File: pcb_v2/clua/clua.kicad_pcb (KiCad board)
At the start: 2 copper layers, 160.7 x 210 mm, 86 parts, among them J1 bus clu 1, J11 UCODE_1, J12 UCODE_2, J13 UCODE_3, J14 UCODE_4, J15 UCODE_5, J16 UCODE_6, J17 UCODE_7, J18 UCODE_INT, J2 bus clu 2, J3 bus clu 3, J4 UCODE_RESET, J7 UCODE_0, SW1 SW_DIP_x04, SW3 SW_DIP_x04, SW6 SW_DIP_x04, U1 74LS193, U10 MC14495P, U11 IR_HIGH, U12 74LS574, U13 74LS244, U15 74LS244, U16 74LS86, U17 74LS125, U18 74LS244, U19 74LS04, U2 74HC238, U20 74LS08, U24 74LS86, U25 74LS125, U26 74LS32, U27 74LS08, U28 74LS74, U29 74LS74, U30 74LS138, U31 MC14495P, U32 74HC238, U4 74LS02, U5 74LS32, U6 74LS157, U7 74LS157, U8 74LS574, U9 IR_LOW

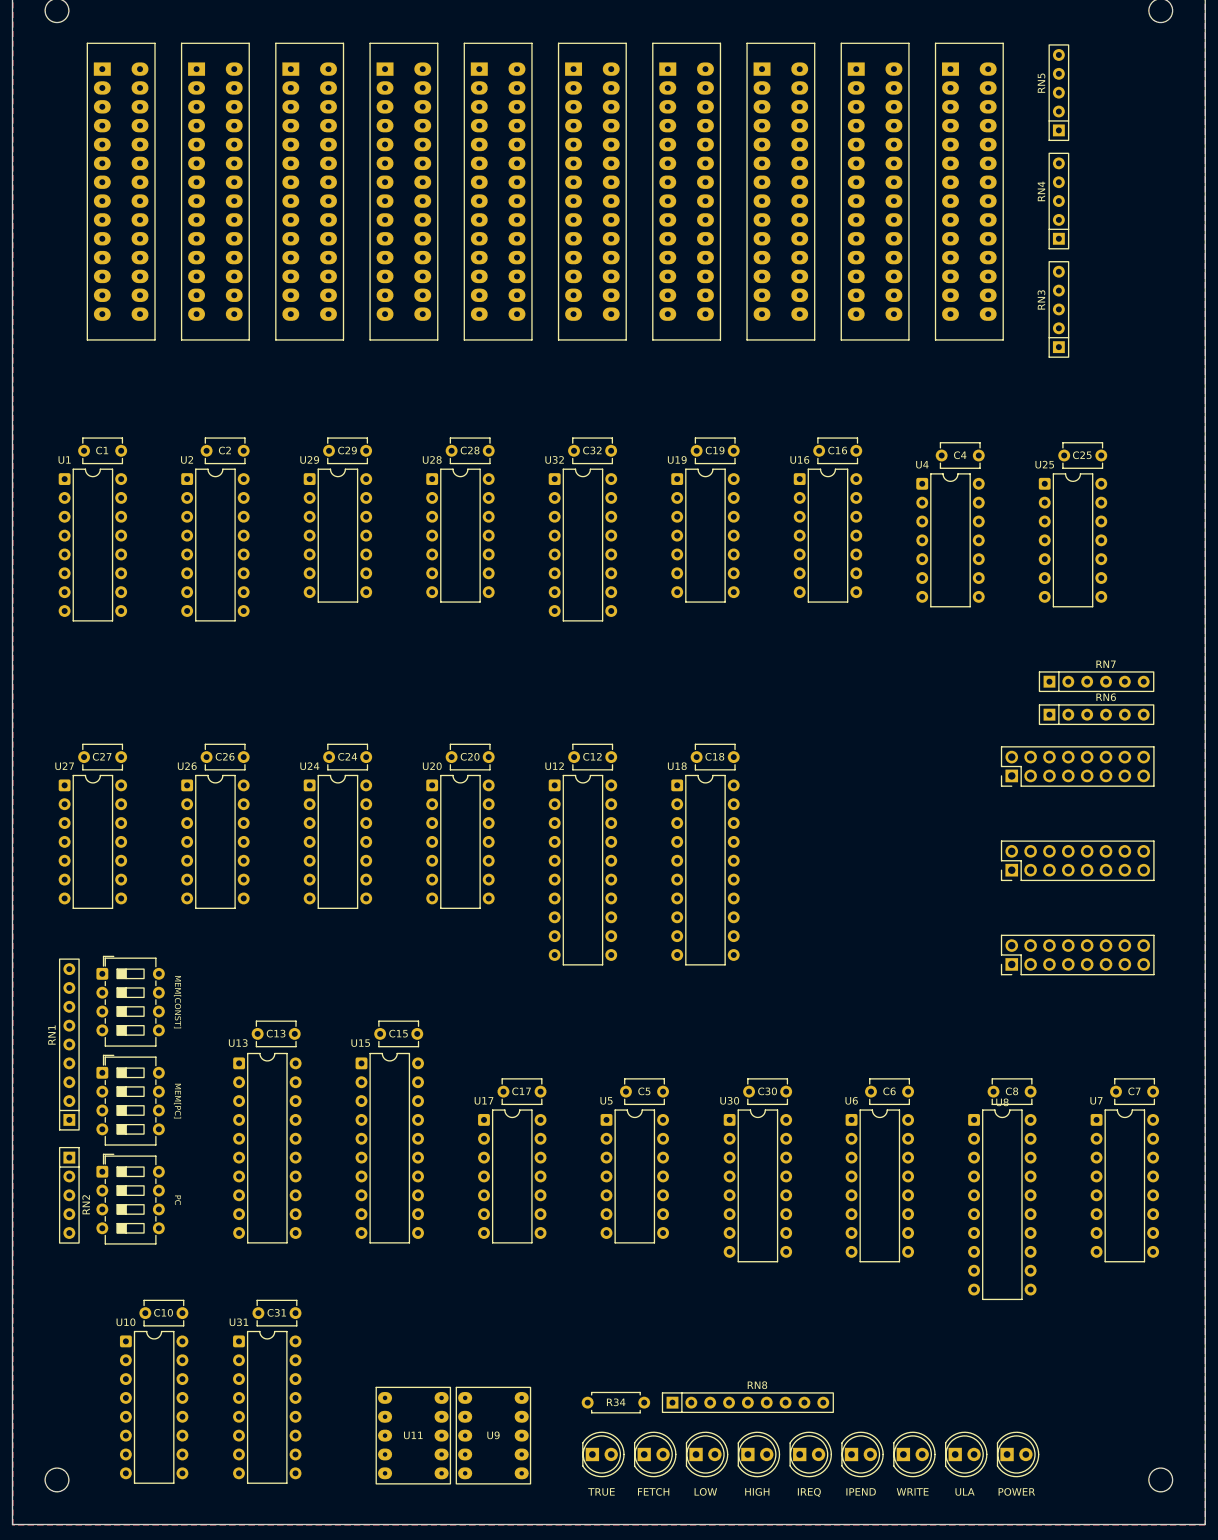
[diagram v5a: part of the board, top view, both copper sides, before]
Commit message: finalizado o layout e testes lógicos do pcb
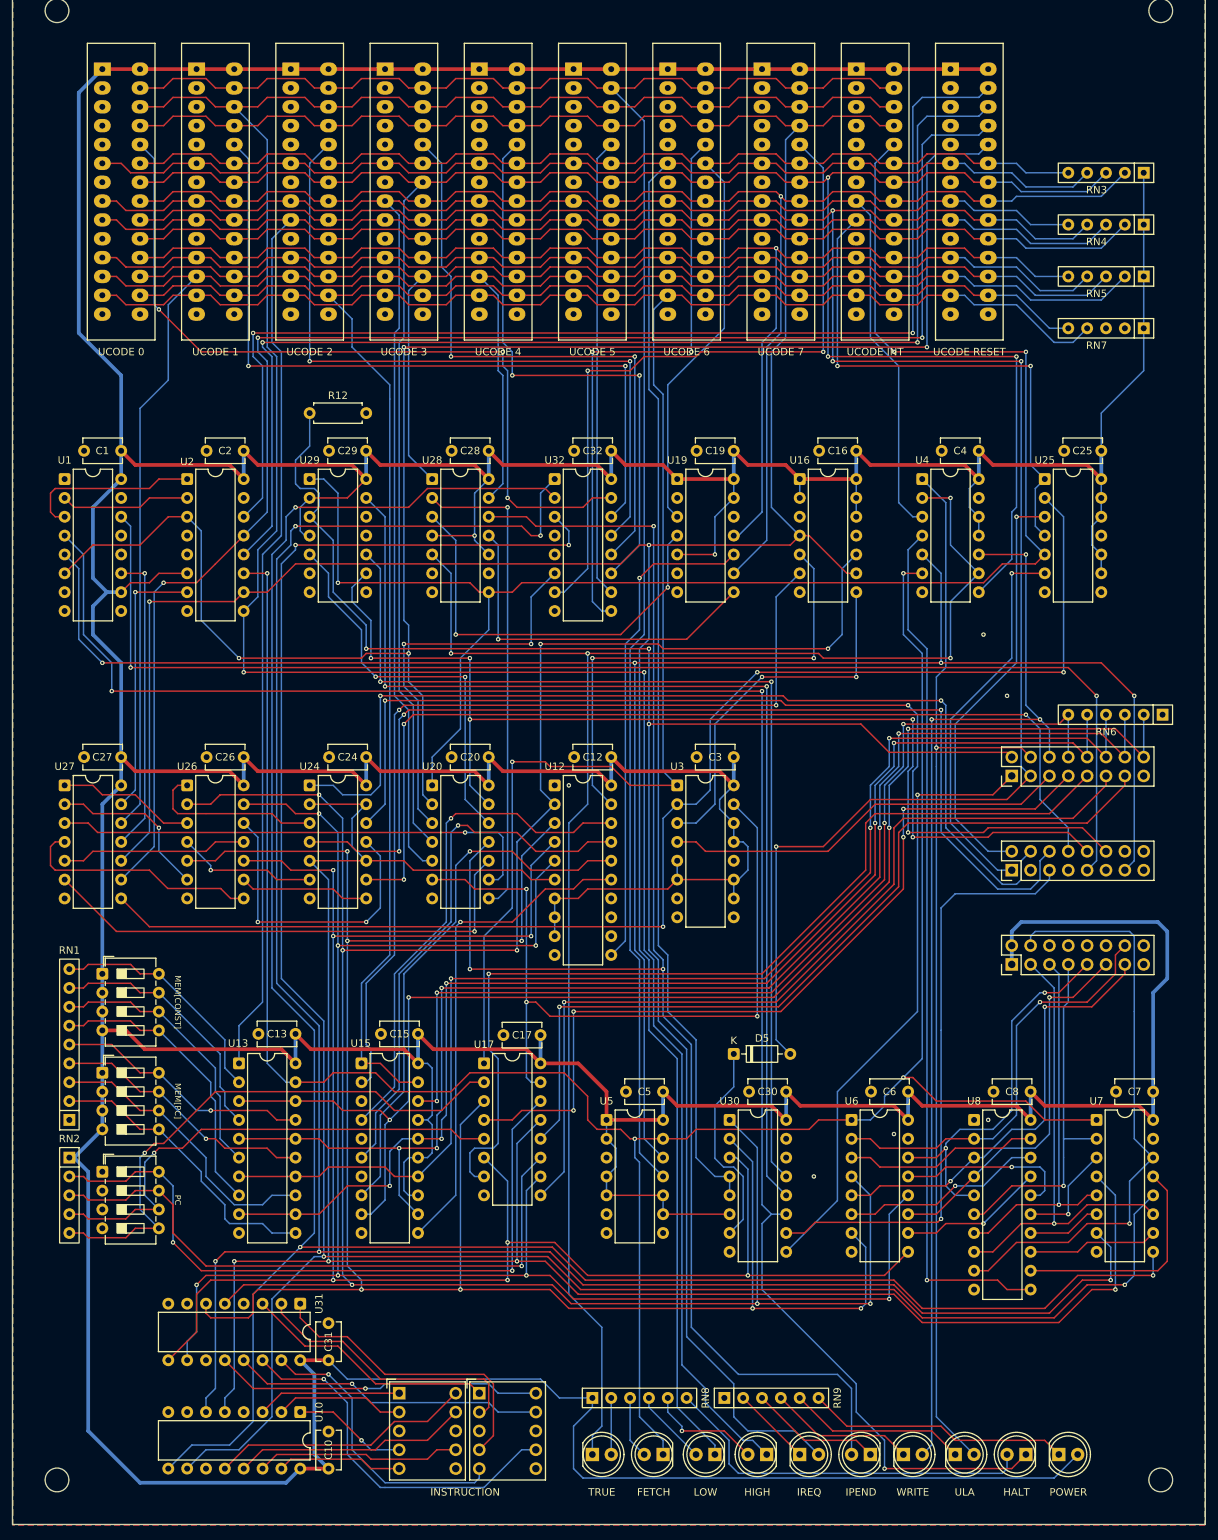
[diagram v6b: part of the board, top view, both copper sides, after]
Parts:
- removed C18: 100nF, Capacitor_THT:C_Disc_D5.1mm_W3.2mm_P5.00mm
- removed J17: UCODE_7, edge_connector:male-edge-connector-28
- removed R34: 1K, Resistor_THT:R_Axial_DIN0207_L6.3mm_D2.5mm_P7.62mm_Horizontal
- removed U18: 74LS244, Package_DIP:DIP-20_W7.62mm
- added C3: 100nF, Capacitor_THT:C_Disc_D5.1mm_W3.2mm_P5.00mm, F.Cu at (111.2, 128.3)
- added D5: 1N4148, Diode_THT:D_DO-35_SOD27_P7.62mm_Horizontal, F.Cu at (116.2, 168.3)
- added D6: HALT, LED_THT:LED_D5.0mm, F.Cu at (155.6, 222.2)
- added J5: UCODE 7, edge_connector:male-edge-connector-28, F.Cu at (120.0, 35.6)
- added R12: 10K, Resistor_THT:R_Axial_DIN0207_L6.3mm_D2.5mm_P7.62mm_Horizontal, F.Cu at (59.1, 81.9)
- added RN9: 1K, Resistor_THT:R_Array_SIP6, F.Cu at (114.9, 214.6)
- added U3: 74LS157, Package_DIP:DIP-16_W7.62mm, F.Cu at (108.6, 132.1)
- J11: value UCODE_1 -> UCODE 1
- J12: value UCODE_2 -> UCODE 2
- J13: value UCODE_3 -> UCODE 3
- J14: value UCODE_4 -> UCODE 4
- J15: value UCODE_5 -> UCODE 5
- J16: value UCODE_6 -> UCODE 6
- J18: value UCODE_INT -> UCODE INT
- J4: value UCODE_RESET -> UCODE RESET
- J7: value UCODE_0 -> UCODE 0
- RN7: footprint Resistor_THT:R_Array_SIP6 -> Resistor_THT:R_Array_SIP5
- RN8: footprint Resistor_THT:R_Array_SIP9 -> Resistor_THT:R_Array_SIP6
- SW1: value SW_DIP_x04 -> SW_DIP_read_mem_const
- SW3: value SW_DIP_x04 -> SW_DIP_mem_pc
- SW6: value SW_DIP_x04 -> SW_DIP_pc
- U11, U9: footprint 7segdisplay:1-digit-13mm -> Display_7Segment:Sx39-1xxxxx
- U17: value 74LS125 -> 74LS157; footprint Package_DIP:DIP-14_W7.62mm -> Package_DIP:DIP-16_W7.62mm
- U2, U32: value 74HC238 -> 74LS138
- moved RN7 49.3 mm to (171.4, 70.5), turned to 180 degrees
- moved C10 29.4 mm to (61.6, 219.2), turned to -90 degrees
- moved RN3 26.1 mm to (171.4, 49.5), turned to 180 degrees
- moved U10 25.4 mm to (57.8, 216.5), turned to -90 degrees
- moved RN5 22.8 mm to (171.4, 63.5), turned to 180 degrees
- moved RN6 15.2 mm to (174.0, 122.6), turned to 180 degrees
- moved RN4 11.6 mm to (171.4, 56.5), turned to 180 degrees
- moved RN8 10.8 mm to (97.2, 214.6)
- moved U31 9.69 mm to (57.8, 201.9), turned to -90 degrees
- moved C31 9.54 mm to (61.6, 204.6), turned to -90 degrees
- moved U17 7.62 mm to (82.5, 169.5)
- moved C17 7.62 mm to (85.2, 165.7)
- moved D1 6.98 mm to (160.0, 222.2)
- moved U11 6.02 mm to (71.1, 214.0)
- moved U9 6.02 mm to (81.9, 214.0)
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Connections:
- net select_opcode_0 renamed ~{select_opcode_0}
- net select_opcode_1 renamed ~{select_opcode_1}
- net select_opcode_2 renamed ~{select_opcode_2}
- net select_opcode_3 renamed ~{select_opcode_3}
- net select_opcode_4 renamed ~{select_opcode_4}
- net select_opcode_5 renamed ~{select_opcode_5}
- net select_opcode_6 renamed ~{select_opcode_6}
- D13 pad 1: Net-(D13-K) -> ~{low_cycle}
- D13 pad 2: low_cycle -> Net-(D13-A)
- D14 pad 1: Net-(D14-K) -> ~{high_cycle}
- D14 pad 2: high_cycle -> Net-(D14-A)
- D2 pad 1: Net-(D2-K) -> ~{fetch_cycle}
- D2 pad 2: fetch_cycle -> Net-(D2-A)
- J11 pad 11: unconnected-(J11-Pin_11-Pad11) -> ~{UC_disable_int}
- J11 pad 16: fetch_clock -> ~{fetch_clock}
- J11 pad 17: high_cycle -> ~{high_cycle}
- J11 pad 18: low_cycle -> ~{low_cycle}
- J11 pad 24: unconnected-(J11-Pin_24-Pad24) -> ~{UC_A}
- J12 pad 11: unconnected-(J12-Pin_11-Pad11) -> ~{UC_disable_int}
- J12 pad 16: fetch_clock -> ~{fetch_clock}
- J12 pad 17: high_cycle -> ~{high_cycle}
- J12 pad 18: low_cycle -> ~{low_cycle}
- J12 pad 24: unconnected-(J12-Pin_24-Pad24) -> ~{UC_A}
- J13 pad 11: unconnected-(J13-Pin_11-Pad11) -> ~{UC_disable_int}
- J13 pad 16: fetch_clock -> ~{fetch_clock}
- J13 pad 17: high_cycle -> ~{high_cycle}
- J13 pad 18: low_cycle -> ~{low_cycle}
- J13 pad 24: unconnected-(J13-Pin_24-Pad24) -> ~{UC_A}
- J14 pad 11: unconnected-(J14-Pin_11-Pad11) -> ~{UC_disable_int}
- J14 pad 16: fetch_clock -> ~{fetch_clock}
- J14 pad 17: high_cycle -> ~{high_cycle}
- J14 pad 18: low_cycle -> ~{low_cycle}
- J14 pad 24: unconnected-(J14-Pin_24-Pad24) -> ~{UC_A}
- J15 pad 11: unconnected-(J15-Pin_11-Pad11) -> ~{UC_disable_int}
- J15 pad 16: fetch_clock -> ~{fetch_clock}
- J15 pad 17: high_cycle -> ~{high_cycle}
- J15 pad 18: low_cycle -> ~{low_cycle}
- J15 pad 24: unconnected-(J15-Pin_24-Pad24) -> ~{UC_A}
- J16 pad 11: unconnected-(J16-Pin_11-Pad11) -> ~{UC_disable_int}
- J16 pad 16: fetch_clock -> ~{fetch_clock}
- J16 pad 17: high_cycle -> ~{high_cycle}
- J16 pad 18: low_cycle -> ~{low_cycle}
- J16 pad 24: unconnected-(J16-Pin_24-Pad24) -> ~{UC_A}
- J18 pad 11: unconnected-(J18-Pin_11-Pad11) -> ~{UC_disable_int}
- J18 pad 16: fetch_clock -> ~{fetch_clock}
- J18 pad 17: high_cycle -> ~{high_cycle}
- J18 pad 18: low_cycle -> ~{low_cycle}
- J18 pad 19: select_opcode_int -> ~{select_opcode_int}
- J18 pad 24: unconnected-(J18-Pin_24-Pad24) -> ~{UC_A}
- J3 pad 15: CLOCK -> unconnected-(J3-Pin_15-Pad15)
- J4 pad 11: unconnected-(J4-Pin_11-Pad11) -> ~{UC_disable_int}
- J4 pad 16: reset_sync -> ~{reset_sync}
- J4 pad 17: reset_high_cycle -> ~{reset_high_cycle}
- J4 pad 18: reset_low_cycle -> ~{reset_low_cycle}
- J4 pad 19: select_opcode_reset -> ~{select_opcode_reset}
- J4 pad 24: unconnected-(J4-Pin_24-Pad24) -> ~{UC_A}
- J7 pad 11: unconnected-(J7-Pin_11-Pad11) -> ~{UC_disable_int}
- J7 pad 16: fetch_clock -> ~{fetch_clock}
- J7 pad 17: high_cycle -> ~{high_cycle}
- J7 pad 18: low_cycle -> ~{low_cycle}
- J7 pad 24: unconnected-(J7-Pin_24-Pad24) -> ~{UC_A}
- RN3 pad 3: ~{UC_save_src_reg} -> ~{UC_write_enable}
- RN3 pad 4: ~{UC_restart_cycle} -> ~{UC_extended_opcode}
- RN4 pad 2: ~{UC_pcia_swap} -> ~{UC_A}
- RN4 pad 3: ~{UC_write_to_pc} -> ~{UC_read_mem_const}
- RN4 pad 4: ~{UC_write_enable} -> ~{UC_pcia_swap}
- RN4 pad 5: ~{UC_clear_cond_reg} -> ~{UC_ula_enable}
- RN5 pad 2: ~{UC_ula_enable} -> ~{UC_restart_cycle}
- RN5 pad 3: ~{UC_extended_opcode} -> ~{UC_clear_cond_reg}
- RN5 pad 4: ~{UC_read_addr_src_reg} -> ~{UC_disable_int}
- RN5 pad 5: ~{UC_read_mem_const} -> ~{UC_save_src_reg}
- RN7 pad 1: GND -> +5V
- RN7 pad 2: WR_ADDR_0 -> unconnected-(RN7-R1-Pad2)
- RN7 pad 3: WR_ADDR_1 -> unconnected-(RN7-R2-Pad3)
- RN7 pad 4: WR_ADDR_2 -> ~{UC_write_to_pc}
- RN7 pad 5: WR_ADDR_3 -> ~{UC_read_addr_src_reg}
- RN8 pad 1: GND -> +5V
- RN8 pad 2: Net-(D4-K) -> Net-(D24-A)
- RN8 pad 3: Net-(D3-K) -> Net-(D2-A)
- RN8 pad 4: Net-(D1-K) -> Net-(D13-A)
- RN8 pad 5: Net-(D27-K) -> Net-(D14-A)
- RN8 pad 6: Net-(D25-K) -> Net-(D6-A)
- SW6 pad 1: +5V -> GND
- SW6 pad 2: +5V -> GND
- SW6 pad 3: +5V -> GND
- SW6 pad 4: +5V -> GND
- U1 pad 1: +5V -> GND
- U1 pad 10: GND -> +5V
- U1 pad 15: +5V -> GND
- U1 pad 4: +5V -> ~{UC_halt}
- U1 pad 6: Net-(U1-QC) -> ~{select_opcode_reset}
- U13 pad 2: Net-(RN1-R5) -> Net-(RN1-R8)
- U13 pad 3: RD_ADDR_1 -> RD_ADDR_4
- U13 pad 4: Net-(RN1-R6) -> Net-(RN1-R7)
- U13 pad 5: RD_ADDR_2 -> RD_ADDR_3
- U13 pad 6: Net-(RN1-R7) -> Net-(RN1-R6)
- U13 pad 7: RD_ADDR_3 -> RD_ADDR_2
- U13 pad 8: Net-(RN1-R8) -> Net-(RN1-R5)
- U13 pad 9: RD_ADDR_4 -> RD_ADDR_1
- U16 pad 4: high_cycle -> ~{low_cycle}
- U16 pad 9: high_cycle -> ~{low_cycle}
- U17 pad 10: ~{UC_write_to_pc} -> INS_{3}
- U17 pad 11: WR_ADDR_1 -> Net-(RN2-R2)
- U17 pad 12: Net-(RN2-R1) -> WR_ADDR_4
- U17 pad 13: ~{UC_write_to_pc} -> INS_{4}
- U17 pad 14: +5V -> Net-(RN2-R1)
- U17 pad 3: WR_ADDR_4 -> INS_{1}
- U17 pad 4: ~{UC_write_to_pc} -> WR_ADDR_1
- U17 pad 6: WR_ADDR_3 -> INS_{2}
- U17 pad 7: GND -> WR_ADDR_2
- U17 pad 8: WR_ADDR_2 -> GND
- U17 pad 9: Net-(RN2-R2) -> WR_ADDR_3
- U19 pad 12: ~{restart_cycle} -> unconnected-(U19-Pad12)
- U19 pad 13: Net-(U2-Y6) -> +5V
- U19 pad 5: fetch_cycle -> +5V
- U19 pad 6: ~{fetch_cycle} -> unconnected-(U19-Pad6)
- U2 pad 10: high_cycle -> ~{low_cycle}
- U2 pad 11: low_cycle -> ~{fetch_cycle}
- U2 pad 12: fetch_cycle -> ~{reset_high_cycle}
- U2 pad 13: reset_high_cycle -> ~{reset_low_cycle}
- U2 pad 14: reset_low_cycle -> ~{reset_sync}
- U2 pad 15: reset_sync -> unconnected-(U2-O0-Pad15)
- U2 pad 3: Net-(U1-QC) -> ~{select_opcode_reset}
- U2 pad 6: ~{UC_halt} -> +5V
- U2 pad 7: unconnected-(U2-Y7-Pad7) -> ~{restart_cycle}
- U2 pad 9: Net-(U2-Y6) -> ~{high_cycle}
- U20 pad 1: +5V -> ~{select_opcode_int}
- U20 pad 11: Net-(U29A-C) -> int_pending
- U20 pad 12: INT_REQUEST -> Net-(U29A-Q)
- U20 pad 2: +5V -> ~{select_opcode_reset}
- U20 pad 3: unconnected-(U20-Pad3) -> Net-(U32-E3)
- U20 pad 6: write_address -> ~{enable_wr_addr}
- U25 pad 11: WR_ADDR_0 -> unconnected-(U25-Pad11)
- U25 pad 12: Net-(U25-Pad12) -> +5V
- U25 pad 13: ~{UC_write_to_pc} -> +5V
- U25 pad 2: Net-(U25-Pad12) -> ~{any_low_cycle}
- U25 pad 5: select_opcode_reset -> ~{select_opcode_int}
- U27 pad 10: fetch_cycle -> ~{low_cycle}
- U27 pad 8: fetch_clock -> ~{any_low_cycle}
- U27 pad 9: CLOCK -> ~{reset_low_cycle}
- U28 pad 8: unconnected-(U28B-~{Q}-Pad8) -> ~{select_opcode_int}
- U28 pad 9: select_opcode_int -> unconnected-(U28B-Q-Pad9)
- U29 pad 1: ~{UC_int_ready} -> ~{select_opcode_int}
- U29 pad 3: Net-(U29A-C) -> INT_REQUEST
- U29 pad 5: int_pending -> Net-(U29A-Q)
- U30 pad 7: unconnected-(U30-O7-Pad7) -> Net-(D5-K)
- U32 pad 4: select_opcode_int -> GND
- U32 pad 5: select_opcode_int -> GND
- U32 pad 7: select_opcode_7 -> ~{select_opcode_7}
- U4 pad 4: Net-(U25-Pad12) -> fetch_clock
- U4 pad 5: reset_low_cycle -> ~{CLOCK}
- U4 pad 6: low_cycle -> ~{fetch_cycle}
- U5 pad 10: high_cycle -> +5V
- U5 pad 11: select_opcode_reset -> ~{fetch_clock}
- U5 pad 12: reset_low_cycle -> ~{CLOCK}
- U5 pad 13: reset_high_cycle -> ~{fetch_cycle}
- U5 pad 4: low_cycle -> +5V
- U5 pad 5: fetch_cycle -> +5V
- U5 pad 6: Net-(U5-Pad6) -> unconnected-(U5-Pad6)
- U5 pad 8: Net-(U32-E3) -> unconnected-(U5-Pad8)
- U5 pad 9: Net-(U5-Pad6) -> +5V
- U6 pad 1: fetch_cycle -> ~{fetch_cycle}
- U6 pad 10: DATA_{2} -> Net-(U6-I1c)
- U6 pad 11: Net-(U6-I0c) -> DATA_{2}
- U6 pad 13: DATA_{3} -> Net-(U6-I1d)
- U6 pad 14: Net-(U6-I0d) -> DATA_{3}
- U6 pad 2: Net-(U6-I0a) -> DATA_{0}
- U6 pad 3: DATA_{0} -> Net-(U6-I1a)
- U6 pad 5: Net-(U6-I0b) -> DATA_{1}
- U6 pad 6: DATA_{1} -> Net-(U6-I1b)
- U7 pad 1: fetch_cycle -> ~{fetch_cycle}
- U7 pad 10: DATA_{6} -> Net-(U7-I1c)
- U7 pad 11: Net-(U7-I0c) -> DATA_{6}
- U7 pad 13: DATA_{7} -> Net-(U7-I1d)
- U7 pad 14: Net-(U7-I0d) -> DATA_{7}
- U7 pad 2: Net-(U7-I0a) -> DATA_{4}
- U7 pad 3: DATA_{4} -> Net-(U7-I1a)
- U7 pad 5: Net-(U7-I0b) -> DATA_{5}
- U7 pad 6: DATA_{5} -> Net-(U7-I1b)
- U8 pad 12: Net-(U7-I0d) -> Net-(U7-I1d)
- U8 pad 13: Net-(U7-I0c) -> Net-(U7-I1c)
- U8 pad 14: Net-(U7-I0b) -> Net-(U7-I1b)
- U8 pad 15: Net-(U7-I0a) -> Net-(U7-I1a)
- U8 pad 16: Net-(U6-I0d) -> Net-(U6-I1d)
- U8 pad 17: Net-(U6-I0c) -> Net-(U6-I1c)
- U8 pad 18: Net-(U6-I0b) -> Net-(U6-I1b)
- U8 pad 19: Net-(U6-I0a) -> Net-(U6-I1a)
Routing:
- net +5V: track 0.00 -> 1251.2 mm, vias 0 -> 2
- net ~{low_cycle}: track 0.00 -> 433.2 mm, vias 0 -> 2
- net ~{high_cycle}: track 0.00 -> 357.4 mm, vias 0 -> 2
- net INS_{0}: track 0.00 -> 340.7 mm, vias 0 -> 8
- net ~{UC_read_mem_const}: track 0.00 -> 336.2 mm, vias 0 -> 2
- net ~{UC_write_enable}: track 0.00 -> 316.7 mm, vias 0 -> 3
- net ~{fetch_cycle}: track 0.00 -> 313.4 mm, vias 0 -> 4
- net ~{UC_pcia_swap}: track 0.00 -> 308.0 mm, vias 0 -> 4
- net INS_{7}: track 0.00 -> 306.9 mm, vias 0 -> 4
- net INS_{6}: track 0.00 -> 304.2 mm, vias 0 -> 3
- net INS_{5}: track 0.00 -> 297.6 mm, vias 0 -> 5
- net ~{UC_extended_opcode}: track 0.00 -> 290.1 mm
- net INS_{4}: track 0.00 -> 287.4 mm, vias 0 -> 4
- net ~{UC_ula_enable}: track 0.00 -> 280.7 mm
- net ~{UC_write_to_pc}: track 0.00 -> 279.5 mm, vias 0 -> 1
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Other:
- board text added: "INSTRUCTION"
